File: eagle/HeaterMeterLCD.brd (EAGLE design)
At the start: 69.8 x 41.3 mm, 21 parts, among them IC3 74HC595N, J1 LCD, Q4 BS170

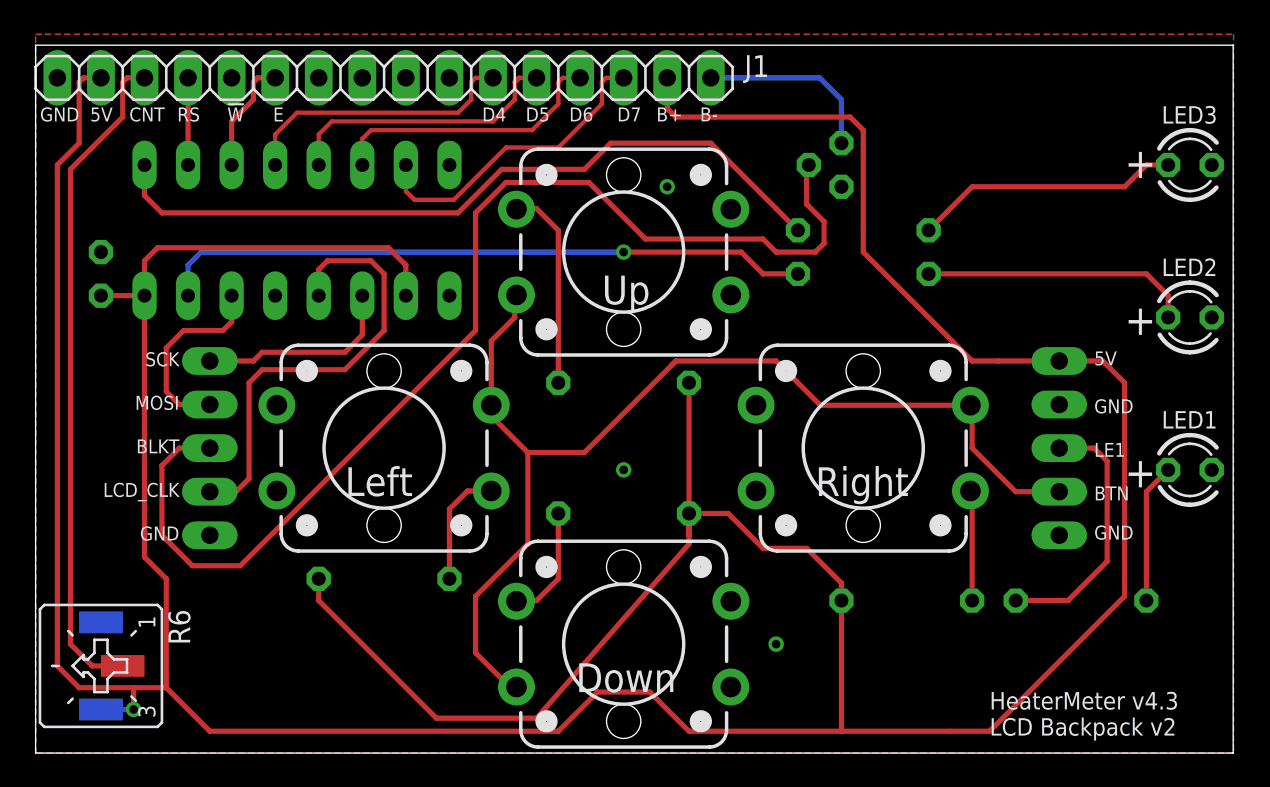
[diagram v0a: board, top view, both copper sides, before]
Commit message: [eagle] HeaterMeter 4.3.4
-- Base Board --
Increase annular ring to 14mil (from 7)
Increase thermal isolation to 15mil (from 10)
Chamfer corners on front edge
Rearrange power MOSFET footprint to sink more heat into board
Add TC+/- indicators to thermocouple pins
More direct path for 5V out and 12V in (swap D3 and R21)

-- LCD Board --
Add word "CONTRAST" by contrast pot
Increase annular ring to 14mil (from 12)
Increase thermals to 15mil (from 10)
Redo LCD1M labels to match labels of MOSI/SCK/etc on main
Add pin labels to shift register
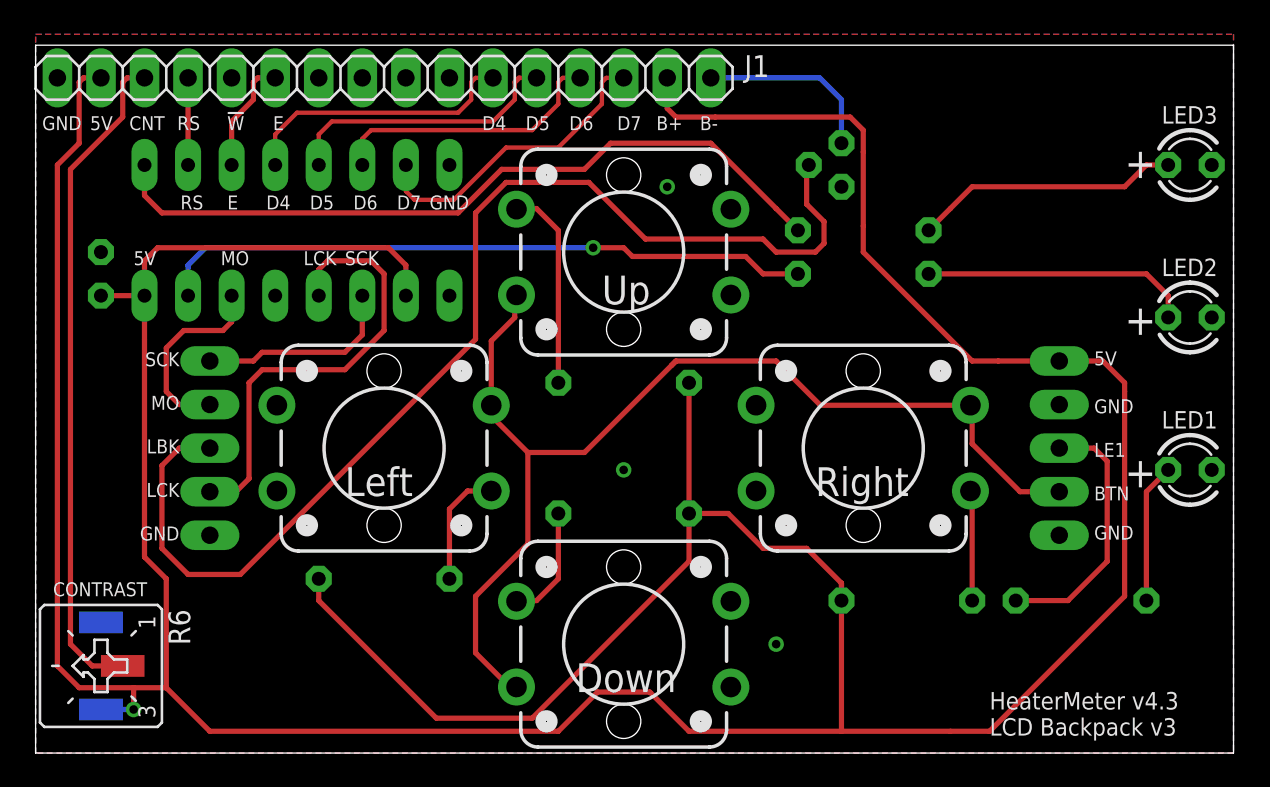
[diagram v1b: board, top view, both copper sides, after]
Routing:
- net LCD_BKLT: track 66.8 -> 68.0 mm
- net +5V: track 266.7 -> 265.6 mm
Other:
- board text added: "CONTRAST"
- board text added: "LBK"
- board text added: "LCD Backpack v3"
- board text added: "LCK"
- board text added: "MO"
- board text removed: "BLKT"
- board text removed: "LCD Backpack v2"
- board text removed: "LCD_CLK"
- board text removed: "MOSI"
